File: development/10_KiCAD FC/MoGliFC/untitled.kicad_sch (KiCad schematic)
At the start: 8 parts

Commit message: schematic update
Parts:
- added C1_LDO1, C1_LDO2: 10u, Capacitor_SMD:C_0805_2012Metric, symbol Device:C_Small
- added C2_LDO1, C2_LDO2: 20u, Capacitor_SMD:C_0805_2012Metric, symbol Device:C_Small
- added C_BECVTX1: 4u7, Capacitor_SMD:C_1206_3216Metric, symbol Device:C_Small
- added C_BECVTX2: 100n, Capacitor_SMD:C_1206_3216Metric, symbol Device:C_Small
- added C_BECVTX3: 1u, Capacitor_SMD:C_1206_3216Metric, symbol Device:C_Small
- added C_BECVTX4, C_BECVTX5, C_BECVTX6: 10u, Capacitor_SMD:C_1206_3216Metric, symbol Device:C_Small
- added D1, D2: B5819W, Diode_SMD:D_SOD-123, symbol Device:D_Schottky_Small
- added R_BECFC3: 12k1, Resistor_SMD:R_0402_1005Metric, symbol Device:R_Small
- added R_BECVTX1: 10k5, Resistor_SMD:R_0402_1005Metric, symbol Device:R_Small
- added R_BECVTX2: 80k6, Resistor_SMD:R_0402_1005Metric, symbol Device:R_Small
- added R_BECVTX3: 10k, Resistor_SMD:R_0402_1005Metric, symbol Device:R_Small
- added U_BEC_VTX_9V_1: TPSM33625RDNR, RDN0011A-MFG, symbol custom_Library:TPSM33625RDNR
- added U_LDO1, U_LDO2: LP5912-3.3DRVR, custom_Library:LP59123.3_SON65P200X200X80-7N, symbol custom_Library:LP5912-3.3DRVR
- C_BECFC4, C_BECFC5: value 47u -> 33u
- R_BECFC1: value 40k2 -> 41k2
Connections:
- net 5V_BEC_FC: now also D1.2 (A)
- net GND: now also C1_LDO1.1, C1_LDO2.1, C2_LDO1.2, C2_LDO2.2, C_BECVTX1.2, C_BECVTX2.2, C_BECVTX3.2, C_BECVTX4.2, C_BECVTX5.2, C_BECVTX6.2, R_BECFC3.2, R_BECVTX1.2, R_BECVTX3.2, U_BEC_VTX_9V_1.10 (GND), U_LDO1.5 (GND), U_LDO1.7 (EXP), U_LDO2.5 (GND), U_LDO2.7 (EXP)
- net Vin_LIPO: now also C_BECVTX1.1, C_BECVTX2.1, U_BEC_VTX_9V_1.2 (EN), U_BEC_VTX_9V_1.3 (VIN)
- net at C_BECFC3.1, U_BEC_FC_5V_1.8 (VCC): no longer U_BEC_FC_5V_1.11 (RT)
- new net: R_BECFC3.1, U_BEC_FC_5V_1.11 (RT)
- new net: R_BECVTX1.1, U_BEC_VTX_9V_1.11 (RT)
- new net: C_BECVTX3.1, U_BEC_VTX_9V_1.8 (VCC)
- new net: R_BECVTX2.2, R_BECVTX3.1, U_BEC_VTX_9V_1.9 (FB)
- new net: U_BEC_VTX_9V_1.5 (SW), U_BEC_VTX_9V_1.6 (SW)
- new net +5V: C1_LDO1.2, C1_LDO2.2, D1.1 (K), D2.1 (K), U_LDO1.4 (EN), U_LDO1.6 (IN), U_LDO2.4 (EN), U_LDO2.6 (IN)
- new net +9V: C_BECVTX4.1, C_BECVTX5.1, C_BECVTX6.1, R_BECVTX2.1, U_BEC_VTX_9V_1.4 (VOUT)
- new net 3V3_MCU: C2_LDO1.1, U_LDO1.1 (OUT)
- new net 3V3_SENS: C2_LDO2.1, U_LDO2.1 (OUT)
- new net 5V_USB: D2.2 (A)
- no-connect marks 2 -> 6
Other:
- note added: "3.3V rail 1: 5V->3.3V LDO - MCU --> max.500mA"
- note added: "3.3V rail 2: 5V->3.3V LDO - onboard max. 140mA(OSD) + ??? - offboard (GPS,...): <100mA --> max xxxmA"
- note added: "9V->80k6; 10V:->90k9"
- note added: "Goal: - Peak to peak noise: <50mV - PSRR >70dB down as low as 1Hz"
- note added: "Power Circuitry 5V FC -> 3.3V"
- note added: "ToDo: - optionally connected to PINIO driven pit switches, and/or jumper pad setups that enable end users to select constant-on or transistor switched behavior, particularly if located to support video transmission systems."
- note added: "VTX: BAT->9V@2.5A (DJI:~1A@9V) TPSM33625RDNR"
- note added: "Vx: BAT->5.2V/6V/7V @4A:"
- note removed: "ToDo: - 10V / 2A - optionally connected to PINIO driven pit switches, and/or jumper pad setups that enable end users to select constant-on or transistor switched behavior, particularly if located to support video transmission systems."
- note removed: "VTX: BAT->10V@2A (DJI:~1A@9V)"
- note removed: "Vx: BAT->5V/6V@4A:"
- moved on the sheet: C_BECFC1, C_BECFC2, C_BECFC3, C_BECFC4, C_BECFC5, R_BECFC1, R_BECFC2, U_BEC_FC_5V_1

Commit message: update all
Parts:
- removed D1, D2: B5819W, Diode_SMD:D_SOD-123, symbol Device:D_Schottky_Small
- added C1_LDO3, C1_LDO4: 4u7, Capacitor_SMD:C_0805_2012Metric, symbol Device:C_Small
- added C2_LDO3, C2_LDO4: 2u2, Capacitor_SMD:C_0805_2012Metric, symbol Device:C_Small
- added D_5V, D_5V_USB: B340A-13-F, custom_Library:Schottky BA340 SMA_L4.4-W2.6-LS5.0-RD, symbol custom_Library:B340A-13-F
- added J_ELRS1: ELRS, Connector_PinHeader_1.27mm:PinHeader_1x02_P1.27mm_Vertical, symbol Connector_Generic:Conn_01x02
- added U_LDO3, U_LDO4: LP5912-3.3DRVR, custom_Library:LP59123.3_SON65P200X200X80-7N, symbol custom_Library:LP5912-3.3DRVR
- C1_LDO1, C1_LDO2: value 10u -> 4u7; # Footprint checked (none) -> -; # Value checked (none) -> -; #LCSC Check (none) -> -; #LCSC Part (none) -> C15850; AVAILABILITY x -> (none); LCSC Part # C15850 -> (none); Price (none) -> -
- C2_LDO1, C2_LDO2: value 20u -> 4u7; # Footprint checked (none) -> -; # Value checked (none) -> -; #LCSC Check (none) -> -; #LCSC Part (none) -> C15850; AVAILABILITY x -> (none); LCSC Part # C15850 -> (none); Price (none) -> -
- C_BECFC1, C_BECFC2, C_BECFC3, C_BECFC4, C_BECFC5, C_BECVTX1, C_BECVTX2, C_BECVTX3, C_BECVTX4, C_BECVTX5, C_BECVTX6, U_BEC_FC_5V_1, U_BEC_VTX_9V_1: # Footprint checked (none) -> -; # Value checked (none) -> -; #LCSC Check (none) -> -; Price (none) -> -
- R_BECFC1, R_BECFC2, R_BECFC3, R_BECVTX1, R_BECVTX2, R_BECVTX3: # Footprint checked (none) -> -; # Value checked (none) -> -; #LCSC Check (none) -> -; #LCSC Part (none) -> C25133; AVAILABILITY x -> (none); LCSC Part # C25133 -> (none); Price (none) -> -
- U_LDO1, U_LDO2: # Footprint checked (none) -> -; # Value checked (none) -> -; #LCSC Check (none) -> -; #LCSC Part (none) -> -; Availability In Stock -> (none); LCSC Part # - -> (none); Price None -> -
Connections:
- net 5V_USB: now also D_5V_USB.2 (A)
- net GND: now also C1_LDO3.1, C1_LDO4.1, C2_LDO3.2, C2_LDO4.2, U_LDO3.5 (GND), U_LDO3.7 (EXP), U_LDO4.5 (GND), U_LDO4.7 (EXP)
- net +5V renamed 5V_BUS
- net 5V_BUS: now also D_5V.1 (K), D_5V_USB.1 (K), J_ELRS1.2 (Pin_2)
- net +9V renamed 9V_VTX_PAD
- net 3V3_MCU renamed 3V3_MCU_OSD
- net 3V3_SENS renamed 3V3_IMU
- net 5V_BEC_FC renamed 5V_BEC
- net 5V_BEC: now also D_5V.2 (A)
- new net 3V3_ELRS1: C2_LDO3.1, U_LDO3.1 (OUT)
- new net 3V3_ELRS2: C2_LDO4.1, U_LDO4.1 (OUT)
- new net 5V_ELRS: C1_LDO3.2, C1_LDO4.2, J_ELRS1.1 (Pin_1), U_LDO3.4 (EN), U_LDO3.6 (IN), U_LDO4.4 (EN), U_LDO4.6 (IN)
- no-connect marks 6 -> 8
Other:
- note added: "---->---->---->----->----->----->----->----->"
- note added: "Diodes: 40V/3A 500mV 850mW"
- note added: "ELRS LDO: 5V FC -> 3V3 @500mA"
- note added: "FC LDO: 5V bus -> 3V3 @500mA"
- note added: "FC: BAT->5.1V@2.5A: TPSM33625RDNR"
- note added: "Power Path"
- note added: "| 3.3V rail 1: | - ESP32 Pico D4 | - RXTX1"
- note added: "| 3.3V rail 1: | - MCU --> max.180mA | - OSD --> max.200mA | - ext. pad requirement: <120mA"
- note added: "| 3.3V rail 2: | - IMU --> max 1mA | - baro, mag --> max. 10mA"
- note added: "| 3.3V rail 2: | - RXTX2"
- note added: "| 9V->80k6; 10V:->90k9 | cont. 2.5A"
- note added: "| Notes: | Cin >= Cout; ceramic | Cin/Cout: 1..10uF / ESR 5..500mΩ"
- note added: "| Notes: | calculation see documentation | from TI WEBENCH pdf"
- note removed: "3.3V rail 1: 5V->3.3V LDO - MCU --> max.500mA"
- note removed: "3.3V rail 2: 5V->3.3V LDO - onboard max. 140mA(OSD) + ??? - offboard (GPS,...): <100mA --> max xxxmA"
- note removed: "9V->80k6; 10V:->90k9"
- note removed: "FC: BAT->5V@2.5A: TPSM33625RDNR"
- note removed: "Power Circuitry 5V FC -> 3.3V"
- moved on the sheet: C1_LDO1, C1_LDO2, C2_LDO1, C2_LDO2, C_BECFC1, C_BECFC2, C_BECFC3, C_BECFC4, C_BECFC5, C_BECVTX1, C_BECVTX2, C_BECVTX3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

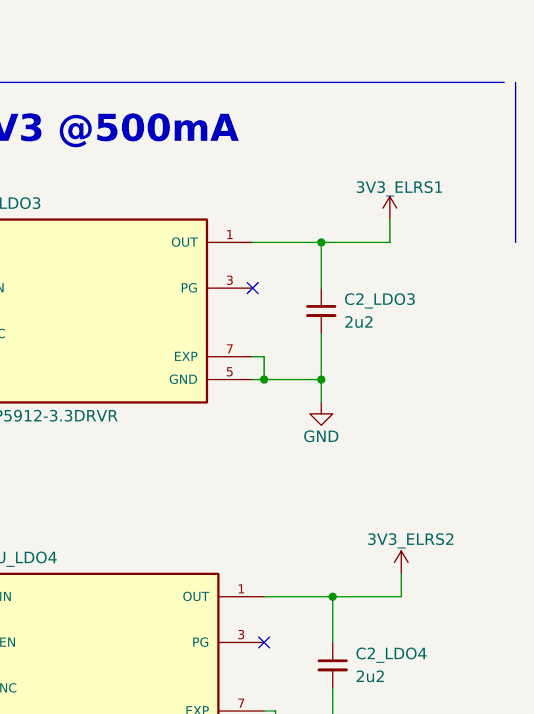
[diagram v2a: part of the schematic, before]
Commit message: schematic update ELRS
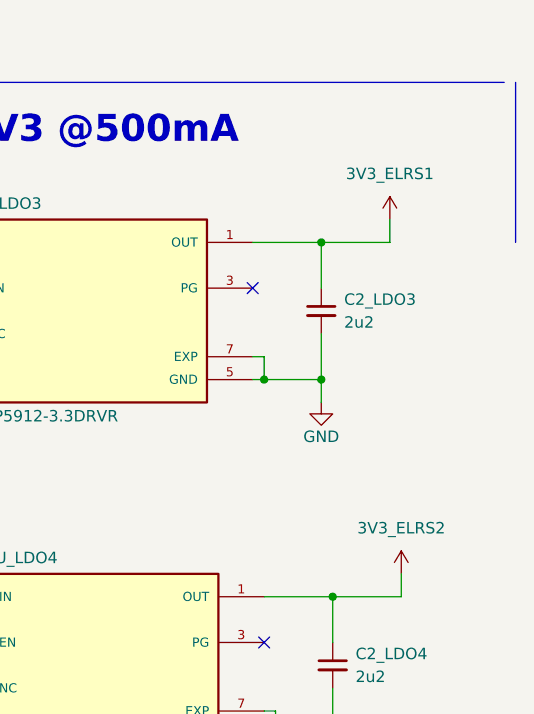
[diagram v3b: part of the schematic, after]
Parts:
- D_5V, D_5V_USB: LCSC Part (none) -> C85098
- U_LDO1, U_LDO2, U_LDO3, U_LDO4: Availability (none) -> In Stock; Price - -> None
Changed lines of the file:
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@@
 	)
 	(symbol
-		(lib_name "LP5912-3.3DRVR_1")
 		(lib_id "custom_Library:LP5912-3.3DRVR")
 		(at 363.22 133.35 0)
@@
 			)
 		)
-		(property "Price" "-"
+		(property "Price" "None"
 			(at 363.22 133.35 0)
 			(effects
@@
 			)
 		)
-		(property "Availability" ""
+		(property "Availability" "In Stock"
 			(at 363.22 133.35 0)
 			(effects
@@
 	)
 	(symbol
-		(lib_id "custom_Library:3V3_SENS")
-		(at 397.51 162.56 0)
+		(lib_id "power:GND")
+		(at 388.62 46.99 0)
 		(unit 1)
 		(exclude_from_sim no)
@@
 		(on_board yes)
 		(dnp no)
-		(property "Reference" "#PWR057"
-			(at 397.51 166.37 0)
+		(property "Reference" "#PWR020"
+			(at 388.62 53.34 0)
 			(effects
 				(font
@@
 			)
 		)
-		(property "Value" "3V3_ELRS2"
-			(at 393.7 158.75 0)
+		(property "Value" "GND"
+			(at 388.62 50.8 0)
 			(effects
 				(font
 					(size 1.27 1.27)
 				)
-				(justify left)
 			)
 		)
 		(property "Footprint" ""
-			(at 397.51 162.56 0)
+			(at 388.62 46.99 0)
 			(effects
 				(font
@@
 		)
 		(property "Datasheet" ""
-			(at 397.51 162.56 0)
+			(at 388.62 46.99 0)
 			(effects
 				(font
@@
 			)
 		)
-		(property "Description" "Power symbol creates a global label with name \"3V3_SENS"
-			(at 397.51 162.56 0)
+		(property "Description" "Power symbol creates a global label with name \"GND\" , ground"
+			(at 388.62 46.99 0)
 			(effects
 				(font
@@
 			(project "MoGliFC"
 				(path "/93ed104c-0023-445d-9c91-226bb47cb218/92026c51-6edb-4a7a-8669-09bc2b3bb2a9"
-					(reference "#PWR057")
+					(reference "#PWR020")
 					(unit 1)
 				)
@@
 	)
 	(symbol
-		(lib_id "power:GND")
-		(at 388.62 46.99 0)
+		(lib_id "custom_Library:3V3_ELRS1")
+		(at 396.24 123.19 0)
 		(unit 1)
 		(exclude_from_sim no)
@@
 		(on_board yes)
 		(dnp no)
-		(property "Reference" "#PWR020"
-			(at 388.62 53.34 0)
+		(fields_autoplaced yes)
+		(property "Reference" "#PWR046"
+			(at 396.24 127 0)
 			(effects
 				(font
@@
 			)
 		)
-		(property "Value" "GND"
-			(at 388.62 50.8 0)
+		(property "Value" "3V3_ELRS1"
+			(at 396.24 118.11 0)
 			(effects
 				(font
@@
 		)
 		(property "Footprint" ""
-			(at 388.62 46.99 0)
+			(at 396.24 123.19 0)
 			(effects
 				(font
@@
 		)
 		(property "Datasheet" ""
-			(at 388.62 46.99 0)
+			(at 396.24 123.19 0)
 			(effects
 				(font
@@
 			)
 		)
-		(property "Description" "Power symbol creates a global label with name \"GND\" , ground"
-			(at 388.62 46.99 0)
+		(property "Description" "Power symbol creates a global label with name \"3V3_ELRS1\""
+			(at 396.24 123.19 0)
 			(effects
 				(font
@@
 		)
 		(instances
-			(project "MoGliFC"
+			(project ""
 				(path "/93ed104c-0023-445d-9c91-226bb47cb218/92026c51-6edb-4a7a-8669-09bc2b3bb2a9"
-					(reference "#PWR020")
+					(reference "#PWR046")
 					(unit 1)
 				)
@@
 			)
 		)
+		(property "LCSC Part" "C85098"
+			(at 77.47 16.51 0)
+			(effects
+				(font
+					(size 1.27 1.27)
+				)
+				(hide yes)
+			)
+		)
 		(pin "1"
 		)
@@
 			)
 		)
-		(property "Price" "-"
+		(property "Price" "None"
 			(at 364.49 172.72 0)
 			(effects
@@
 			)
 		)
-		(property "Availability" ""
+		(property "Availability" "In Stock"
 			(at 364.49 172.72 0)
 			(effects
@@
 			)
 		)
-		(property "Price" "-"
+		(property "Price" "None"
 			(at 364.49 76.2 0)
 			(effects
@@
 			)
 		)
-		(property "Availability" ""
+		(property "Availability" "In Stock"
 			(at 364.49 76.2 0)
 			(effects
@@
 	)
 	(symbol
-		(lib_id "custom_Library:3V3_MCU")
-		(at 396.24 123.19 0)
-		(unit 1)
-		(exclude_from_sim no)
-		(in_bom yes)
-		(on_board yes)
-		(dnp no)
-		(property "Reference" "#PWR046"
-			(at 396.24 127 0)
-			(effects
-				(font
-					(size 1.27 1.27)
-				)
-				(hide yes)
-			)
-		)
-		(property "Value" "3V3_ELRS1"
-			(at 392.43 119.634 0)
-			(effects
-				(font
-					(size 1.27 1.27)
-				)
-				(justify left)
-			)
-		)
-		(property "Footprint" ""
-			(at 396.24 123.19 0)
-			(effects
-				(font
-					(size 1.27 1.27)
-				)
-				(hide yes)
-			)
-		)
-		(property "Datasheet" ""
-			(at 396.24 123.19 0)
-			(effects
-				(font
-					(size 1.27 1.27)
-				)
-				(hide yes)
-			)
-		)
-		(property "Description" "Power symbol creates a global label with name \"3V3_MCU\""
-			(at 396.24 123.19 0)
-			(effects
-				(font
-					(size 1.27 1.27)
-				)
-				(hide yes)
-			)
-		)
-		(pin "1"
-		)
-		(instances
-			(project "MoGliFC"
-				(path "/93ed104c-0023-445d-9c91-226bb47cb218/92026c51-6edb-4a7a-8669-09bc2b3bb2a9"
-					(reference "#PWR046")
-					(unit 1)
-				)
-			)
-		)
-	)
-	(symbol
 		(lib_id "Device:R_Small")
 		(at 256.54 60.96 0)
@@
 	)
 	(symbol
-		(lib_name "LP5912-3.3DRVR_1")
 		(lib_id "custom_Library:LP5912-3.3DRVR")
 		(at 363.22 36.83 0)
@@
 			)
 		)
-		(property "Price" "-"
+		(property "Price" "None"
 			(at 363.22 36.83 0)
 			(effects
@@
 			)
 		)
-		(property "Availability" ""
+		(property "Availability" "In Stock"
 			(at 363.22 36.83 0)
 			(effects
@@
 			)
 		)
+		(property "LCSC Part" "C85098"
+			(at 77.47 30.48 0)
+			(effects
+				(font
+					(size 1.27 1.27)
+				)
+				(hide yes)
+			)
+		)
 		(pin "1"
 		)
@@
 					(unit 1)
 				)
+			)
+		)
+	)
+	(symbol
+		(lib_id "custom_Library:3V3_ELRS2")
+		(at 397.51 162.56 0)
+		(unit 1)
+		(exclude_from_sim no)
+		(in_bom yes)
+		(on_board yes)
+		(dnp no)
+		(fields_autoplaced yes)
+		(property "Reference" "#PWR057"
+			(at 397.51 166.37 0)
+			(effects
+				(font
+					(size 1.27 1.27)
+				)
+				(hide yes)
+			)
+		)
+		(property "Value" "3V3_ELRS2"
+			(at 397.51 157.48 0)
+			(effects
+				(font
+					(size 1.27 1.27)
+				)
+			)
+		)
+		(property "Footprint" ""
+			(at 397.51 162.56 0)
+			(effects
+				(font
+					(size 1.27 1.27)
+				)
+				(hide yes)
+			)
+		)
+		(property "Datasheet" ""
+			(at 397.51 162.56 0)
+			(effects
+				(font
+					(size 1.27 1.27)
+				)
+				(hide yes)
+			)
+		)
+		(property "Description" "Power symbol creates a global label with name \"3V3_ELRS2\""
+			(at 397.51 162.56 0)
+			(effects
+				(font
+					(size 1.27 1.27)
+				)
+				(hide yes)
+			)
+		)
+		(pin "1"
+		)
+		(instances
+			(project ""
+				(path "/93ed104c-0023-445d-9c91-226bb47cb218/92026c51-6edb-4a7a-8669-09bc2b3bb2a9"
+					(reference "#PWR057")
+					(unit 1)
+				)
